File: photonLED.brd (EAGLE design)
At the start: 37.6 x 100 mm, 15 parts, among them T1 MJD32C, T2 MJD32C, T3 MJD32C, T4 MJD32C

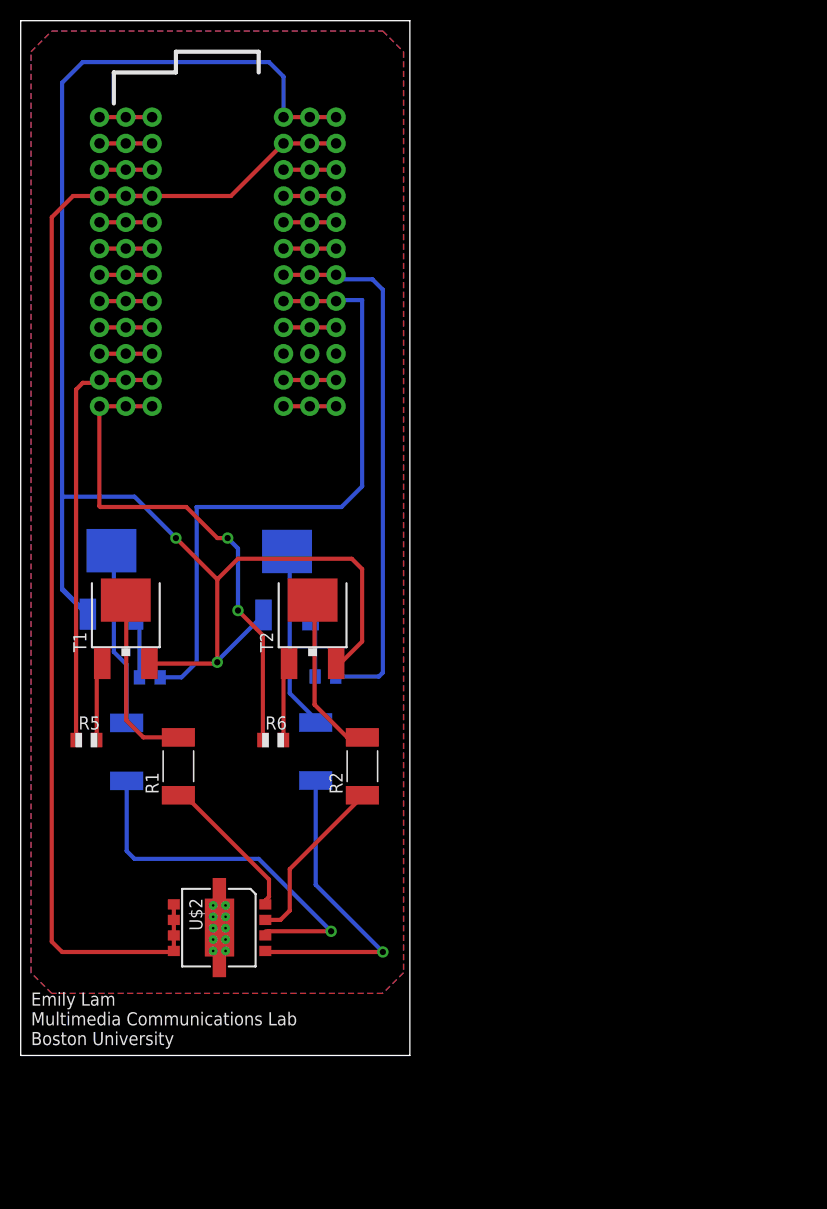
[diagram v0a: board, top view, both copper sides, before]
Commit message: added voltage regulator, DC terminals, all on one side.
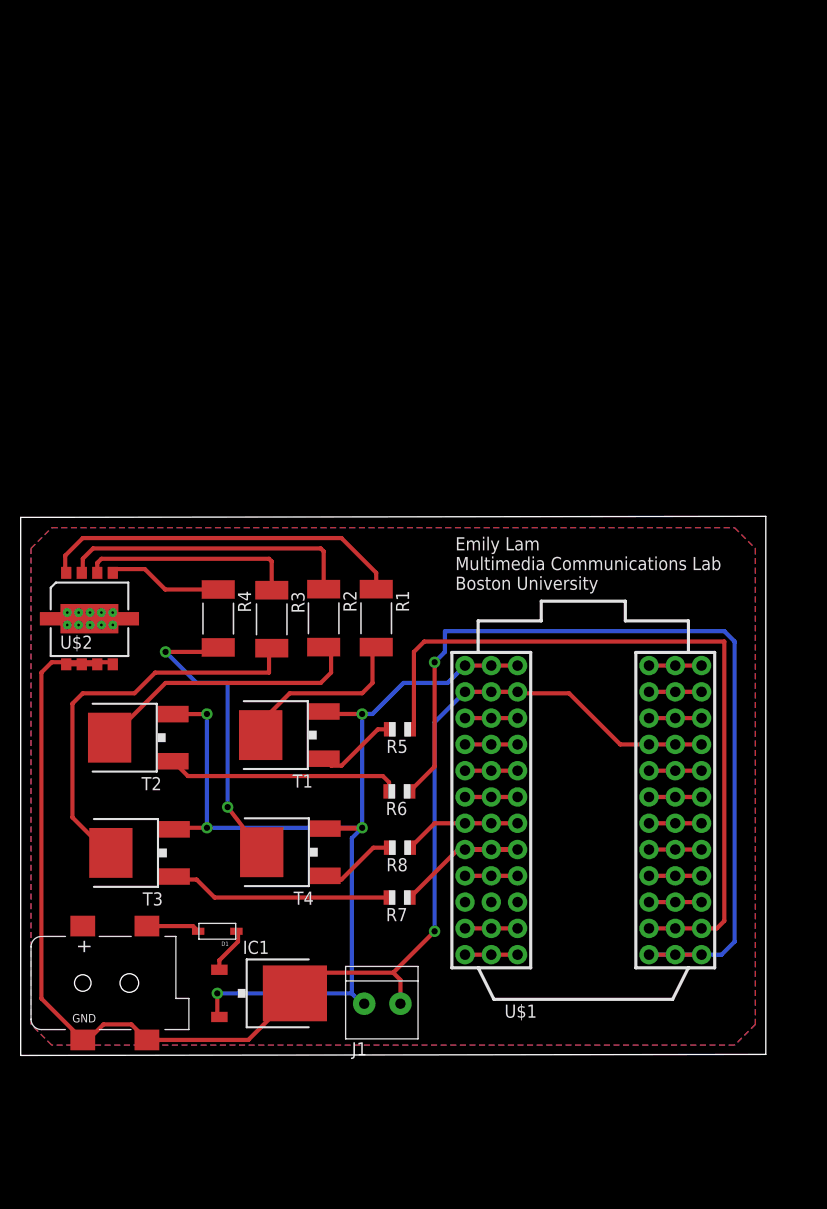
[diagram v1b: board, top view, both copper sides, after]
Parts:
- added D1: (no value), adafruit:SOD-123
- added IC1: 7805DT, adafruit:TO252
- added J1: 3.5MM Screw Term, adafruit:1X2-3.5MM
- added U$3: 2.1MMJACKSMT, adafruit:DCJACK_2MM_SMT
- moved U$1 55.1 mm to (44.2, 5.42), flipped to the top
- moved R7 32.2 mm to (36.6, 15.3), flipped to the top, turned to 180 degrees
- moved R5 30.3 mm to (36.6, 31.5), turned to 180 degrees
- moved T3 27.2 mm to (10.8, 19.6), flipped to the top, turned to 90 degrees
- moved T4 27.0 mm to (25.4, 19.6), flipped to the top, turned to 90 degrees
- moved U$2 24.4 mm to (3.90, 37.2), turned to 0 degrees
- moved R1 23.9 mm to (34.4, 42.3), turned to 270 degrees
- moved T2 20.8 mm to (10.7, 30.7), turned to 90 degrees
- moved R3 19.0 mm to (24.3, 42.2), flipped to the top, turned to 270 degrees
- moved T1 18.7 mm to (25.3, 31.0), turned to 90 degrees
- moved R8 18.0 mm to (36.6, 20.1), flipped to the top, turned to 180 degrees
- moved R4 15.9 mm to (19.1, 42.2), flipped to the top, turned to 270 degrees
- moved R2 14.8 mm to (29.3, 42.3), turned to 270 degrees
- moved R6 13.2 mm to (36.6, 25.5), turned to 180 degrees
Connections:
- new net N$10: D1.C, IC1.1
- new net N$9: D1.A, U$3.PWR2
- net GND: now also IC1.3, J1.2, U$3.GND, U$3.GNDBREAK
- net VIN: now also IC1.2, J1.1
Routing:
- net VIN: track 152.8 -> 104.8 mm, vias 2 -> 5
- net B_LED: track 61.6 -> 17.4 mm
- net W_LED: track 51.9 -> 11.3 mm
- net G_LED: track 49.3 -> 88.2 mm, vias 2 -> 1
- net R_LED: track 41.6 -> 72.6 mm
- net N$7: track 17.3 -> 38.8 mm
- net N$1: track 14.7 -> 35.4 mm
- net N$4: track 30.7 -> 11.2 mm, vias 1 -> 0
- net GND: track 122.3 -> 140.3 mm, vias 0 -> 1
- net N$3: track 36.6 -> 20.9 mm, vias 1 -> 0
- net N$34: track 6.29 -> 21.6 mm
- net N$33: track 7.61 -> 22.6 mm
- net N$8: track 17.7 -> 30.0 mm, vias 0 -> 2
- net N$2: track 16.8 -> 28.9 mm
- net N$6: track 16.1 -> 26.8 mm
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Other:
- board size 37.6 x 100 mm -> 72 x 52.1 mm

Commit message: added color sensor, mounting holes, ground planes, etc.
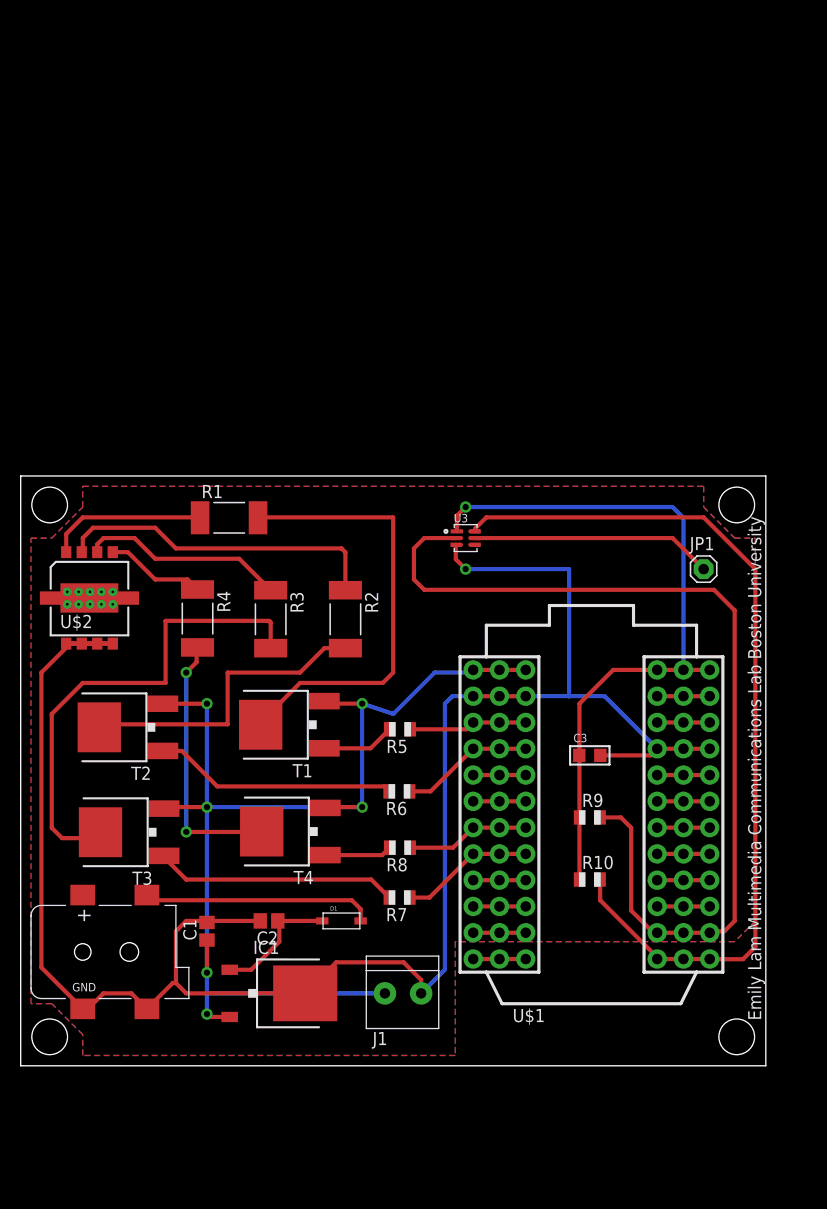
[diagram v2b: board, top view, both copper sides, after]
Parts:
- added C1, C2: 100u, adafruit:C0805
- added C3: 0.1µF, microbuilder:_0805
- added JP1: (no value), adafruit:1X01
- added R10, R9: 1k, adafruit:R0805
- added U3: TCS34725, microbuilder:TCS3472_FN6
- U$1: value Photon -> (none)
- moved R1 17.2 mm to (20.1, 52.0), turned to 0 degrees
- moved D1 12.0 mm to (31.0, 13.0), turned to 0 degrees
- moved U$3 3.00 mm to (6.00, 10.0)
- moved J1 2.24 mm to (37.0, 6.00)
- moved T3 2.24 mm to (9.81, 21.6)
- moved R2 2.10 mm to (31.4, 42.2)
- moved R4 2.00 mm to (17.1, 42.2)
- moved T4 2.00 mm to (25.4, 21.6)
- moved U$2 2.00 mm to (3.90, 39.2)
- moved T2 1.41 mm to (9.69, 31.7)
- moved IC1 1.00 mm to (25.0, 6.00)
- moved T1 1.00 mm to (25.3, 32.0)
- moved U$1 0.89 mm to (45.0, 5.00)
- moved R3 0.10 mm to (24.2, 42.2)
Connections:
- removed net N$21: U$1.#24, U$1.24, U$1.@24
- new net 3V3: C3.1, R10.1, R9.1, U$1.#24, U$1.24, U$1.@24, U3.P$1
- new net SCL: R9.2, U$1.#14, U$1.14, U$1.@14, U3.P$2
- new net SDA: R10.2, U$1.#13, U$1.13, U$1.@13, U3.P$6
- net GND: now also C1.2, C2.2, C3.2, U3.P$3
- net G_LED: now also U$1.#4, U$1.4, U$1.@4; no longer U$1.#13, U$1.13, U$1.@13
- net N$10: now also C2.1
- net N$11: now also JP1.1, U3.P$5; no longer U$1.#3, U$1.3, U$1.@3
- net N$12: now also U$1.#10, U$1.10, U$1.@10; no longer U$1.#4, U$1.4, U$1.@4
- net R_LED: now also U$1.#3, U$1.3, U$1.@3; no longer U$1.#14, U$1.14, U$1.@14
- net VIN: now also C1.1
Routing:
- net SCL: track 0.00 -> 92.5 mm
- net SDA: track 0.00 -> 86.3 mm
- net G_LED: track 88.2 -> 12.9 mm, vias 1 -> 0
- net 3V3: track 0.00 -> 69.8 mm, vias 0 -> 1
- net R_LED: track 72.6 -> 11.4 mm
- net GND: track 140.3 -> 186.8 mm
- net N$5: track 17.2 -> 43.1 mm
- net N$1: track 35.4 -> 15.4 mm
- net N$11: track 5.08 -> 23.3 mm
- net N$9: track 5.16 -> 22.4 mm
- net N$7: track 38.8 -> 47.3 mm
- net N$10: track 4.53 -> 12.3 mm
- net VIN: track 104.8 -> 111.3 mm, vias 5 -> 6
- net N$15: track 0.00 -> 5.10 mm
- net N$12: track 5.08 -> 0.00 mm
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- added copper zone on layer 1, net N$16
- removed copper zone on layer 1, net GND
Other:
- board size 72 x 52.1 mm -> 72 x 57 mm

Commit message: final board layout
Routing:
- net GND: track 186.8 -> 185.7 mm

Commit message: final board
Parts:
- R10, R9: value 1k -> 4.7k
- T1, T2, T3, T4: value MJD32C -> MJD31C
- moved U$1 46.7 mm to (46.7, 51.7), flipped to the bottom, turned to 180 degrees
- moved U3 44.8 mm to (59.9, 8.55)
- moved JP1 35.1 mm to (69.0, 12.0)
- moved R10 24.1 mm to (57.0, 41.0)
- moved T1 20.3 mm to (7.59, 22.1)
- moved T3 13.4 mm to (23.2, 22.1)
- moved R9 12.2 mm to (57.0, 35.0)
- moved R8 12.0 mm to (36.6, 32.1)
- moved T4 10.3 mm to (23.3, 31.7)
- moved R7 7.00 mm to (36.6, 22.3)
- moved D1 6.08 mm to (37.0, 14.0)
- moved R5 5.29 mm to (36.6, 36.8)
- moved C2 5.10 mm to (29.0, 14.0)
- moved C1 3.61 mm to (21.0, 14.0), turned to 0 degrees
- moved T2 2.05 mm to (7.64, 31.7)
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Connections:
- removed net N$13: U$1.#5, U$1.5, U$1.@5
- removed net N$6 (its old number): R2.2, T2.4
- new net N$15: U$1.#4, U$1.4, U$1.@4
- new net N$18: T4.4, U$2.5
- net B_LED: now also U$1.#3, U$1.3, U$1.@3; no longer U$1.#8, U$1.8, U$1.@8
- net GND: now also T1.3, T2.3, T3.3, T4.3; no longer U$2.5, U$2.6, U$2.7, U$2.8
- net G_LED: now also U$1.#5, U$1.5, U$1.@5; no longer U$1.#4, U$1.4, U$1.@4
- net N$5: now also U$2.8; no longer R1.2
- net N$7: now also T2.4, U$2.7; no longer R3.2, T3.4
- net N$8: now also T3.4, U$2.6; no longer R4.2, T4.4
- net R_LED: now also U$1.#8, U$1.8, U$1.@8; no longer U$1.#3, U$1.3, U$1.@3
- net VIN: now also R1.2, R2.2, R3.2, R4.2; no longer T1.3, T2.3, T3.3, T4.3
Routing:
- net GND: track 185.7 -> 56.0 mm, vias 1 -> 0
- net N$7: track 47.3 -> 8.26 mm
- net N$32: track 7.08 -> 43.4 mm, vias 0 -> 2
- net N$6 (its old number): track 29.9 -> 0.00 mm
- net 3V3: track 69.8 -> 42.6 mm
- net SDA: track 86.3 -> 60.6 mm
- net N$9: track 22.4 -> 46.8 mm, vias 0 -> 1
- net SCL: track 92.5 -> 68.7 mm, vias 0 -> 1
- net N$5: track 43.1 -> 21.7 mm
- net N$18: track 0.00 -> 17.4 mm
- net VIN: track 111.3 -> 127.5 mm, vias 6 -> 1
- net N$34: track 23.5 -> 9.34 mm
- net N$11: track 23.3 -> 10.7 mm
- net N$10: track 12.3 -> 19.4 mm
- net N$8: track 26.6 -> 30.1 mm, vias 2 -> 0
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- added copper zone on layer 1, net GND
- removed copper zone on layer 1, net N$16
